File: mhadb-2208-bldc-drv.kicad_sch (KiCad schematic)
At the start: 0 parts

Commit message: schem: import STM32F103C8Tx from line sensor
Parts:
- added C10, C11, C5, C8, C9: 0u1, Capacitor_SMD:C_0402_1005Metric, symbol Device:C
- added C12, C13: 1u, Capacitor_SMD:C_0402_1005Metric, symbol Device:C
- added C14: 10n, Capacitor_SMD:C_0402_1005Metric, symbol Device:C
- added C4: 10u, Capacitor_SMD:C_0805_2012Metric, symbol Device:C
- added C6, C7: 20p, Capacitor_SMD:C_0603_1608Metric, symbol Device:C
- added D11: YELLOW, LED_SMD:LED_0805_2012Metric, symbol Device:LED
- added FB1: 600Ω@100M, Inductor_SMD:L_0805_2012Metric, symbol Device:FerriteBead
- added J2, J4: Conn_01x04_Pin, Connector_PinHeader_2.54mm:PinHeader_1x04_P2.54mm_Vertical, symbol Connector:Conn_01x04_Pin
- added R4: 10k, Resistor_SMD:R_0402_1005Metric, symbol Device:R
- added R5: 560, Resistor_SMD:R_0603_1608Metric, symbol Device:R_Small
- added R6: 5k1, Resistor_SMD:R_0402_1005Metric, symbol Device:R
- added TP4, TP5, TP6, TP7: TestPoint, TestPoint:TestPoint_Pad_D2.0mm, symbol Connector:TestPoint
- added U3: STM32F103C8Tx, Package_QFP:LQFP-48_7x7mm_P0.5mm, symbol MCU_ST_STM32F1:STM32F103C8Tx
- added Y1: 8M, Crystal:Crystal_SMD_5032-2Pin_5.0x3.2mm, symbol Device:Crystal
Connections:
- new net: R6.1, U3.38 (PA15)
- new net: D11.2 (A), R6.2
- new net: J2.3 (Pin_3), U3.21 (PB10)
- new net: J2.4 (Pin_4), U3.22 (PB11)
- new net: J2.1 (Pin_1), U3.45 (PB8)
- new net: J2.2 (Pin_2), U3.46 (PB9)
- new net: C13.1, C14.1, FB1.1, TP6.1, U3.9 (VDDA)
- new net +3V3: C10.1, C11.1, C12.1, C4.1, C8.1, C9.1, FB1.2, J4.1 (Pin_1), U3.1 (VBAT), U3.24 (VDD), U3.36 (VDD), U3.48 (VDD)
- new net BOOT: R4.2, U3.44 (BOOT0)
- new net BTN1: U3.43 (PB7)
- new net BTN2: U3.42 (PB6)
- new net CAN_RX: U3.32 (PA11)
- new net CAN_TX: U3.33 (PA12)
- new net GND: C10.2, C11.2, C12.2, C13.2, C14.2, C4.2, C5.2, C6.2, C7.2, C8.2, C9.2, D11.1 (K), J4.3 (Pin_3), R4.1, U3.23 (VSS), U3.35 (VSS), U3.47 (VSS), U3.8 (VSSA)
- new net LS1: TP7.1, U3.10 (PA0)
- new net LS10: TP4.1, U3.19 (PB1)
- new net LS2: U3.11 (PA1)
- new net LS3: U3.12 (PA2)
- new net LS4: U3.13 (PA3)
- new net LS5: U3.14 (PA4)
- new net LS6: U3.15 (PA5)
- new net LS7: U3.16 (PA6)
- new net LS8: U3.17 (PA7)
- new net LS9: U3.18 (PB0)
- new net NRST: C5.1, TP5.1, U3.7 (NRST)
- new net RGB1: U3.25 (PB12)
- new net RGB2: U3.26 (PB13)
- new net SWCLK: U3.37 (PA14)
- new net SWDIO: U3.34 (PA13)
- new net SWO: U3.39 (PB3)
- new net U0RXD: J4.2 (Pin_2), U3.31 (PA10)
- new net U0TXD: J4.4 (Pin_4), U3.30 (PA9)
- new net XTAL_I: C6.1, U3.5 (PD0), Y1.2
- new net XTAL_O: R5.2, U3.6 (PD1)
- new net XTAL_RO: C7.1, R5.1, Y1.1
- no-connect marks 0 -> 9
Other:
- note added: "CAN Alive"
- note added: "HSE"
- note added: "UART"

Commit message: schem: add buttons
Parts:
- removed TP4, TP7: TestPoint, TestPoint:TestPoint_Pad_D2.0mm, symbol Connector:TestPoint
- added SW1, SW4: SW_Push, Button_Switch_SMD:SW_SPST_TS-1088-xR020, symbol Switch:SW_Push
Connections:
- net +3V3: now also SW1.1
- net BOOT: now also SW1.2
- net GND: now also SW4.1
- net NRST: now also SW4.2
- net BTN1: no longer names the net of U3.43 (PB7)
- net BTN2: no longer names the net of U3.42 (PB6)
- net LS1: no longer names the net of U3.10 (PA0)
- net LS10: no longer names the net of U3.19 (PB1)
- net LS2: no longer names the net of U3.11 (PA1)
- net LS3: no longer names the net of U3.12 (PA2)
- net LS4: no longer names the net of U3.13 (PA3)
- net LS5: no longer names the net of U3.14 (PA4)
- net LS6: no longer names the net of U3.15 (PA5)
- net LS7: no longer names the net of U3.16 (PA6)
- net LS8: no longer names the net of U3.17 (PA7)
- net LS9: no longer names the net of U3.18 (PB0)
- net RGB2: no longer names the net of U3.26 (PB13)
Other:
- note added: "Buttons"

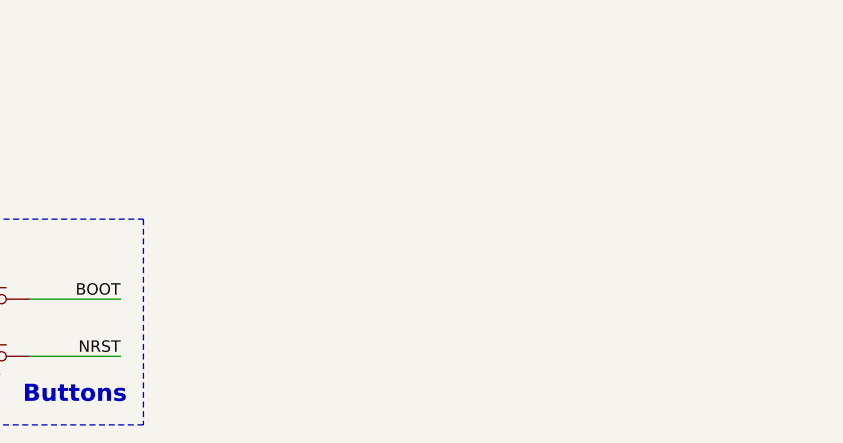
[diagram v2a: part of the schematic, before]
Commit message: schem: add CAN/Power connector
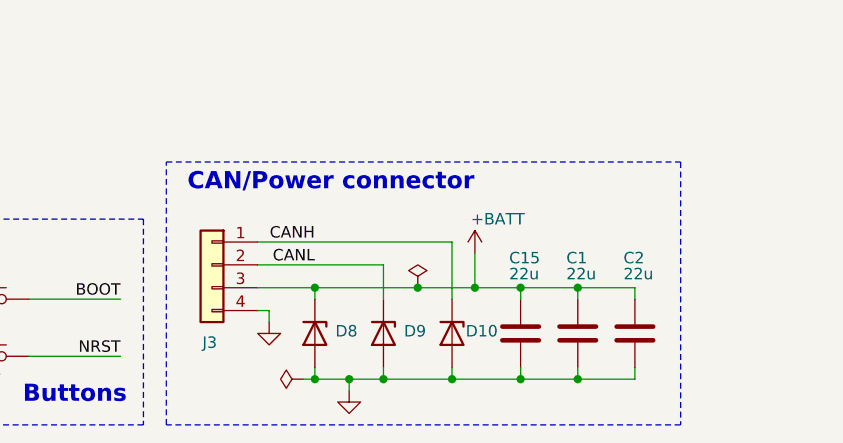
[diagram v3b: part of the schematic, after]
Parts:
- added C1, C15, C2: 22u, Capacitor_SMD:C_1206_3216Metric, symbol Device:C
- added D10, D8, D9: H5VU10U, GLCS:Diode_DFN1006, symbol GLCS:H5VU10U
- added J3: Conn_01x04, Connector_JST:JST_PH_S4B-PH-K_1x04_P2.00mm_Horizontal, symbol Connector_Generic:Conn_01x04
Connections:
- net GND: now also C1.2, C15.2, C2.2, D10.2 (A), D8.2 (A), D9.2 (A), J3.4 (Pin_4)
- new net +BATT: C1.1, C15.1, C2.1, D8.1 (K), J3.3 (Pin_3)
- new net CANH: D10.1 (K), J3.1 (Pin_1)
- new net CANL: D9.1 (K), J3.2 (Pin_2)
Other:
- note added: "CAN/Power connector"

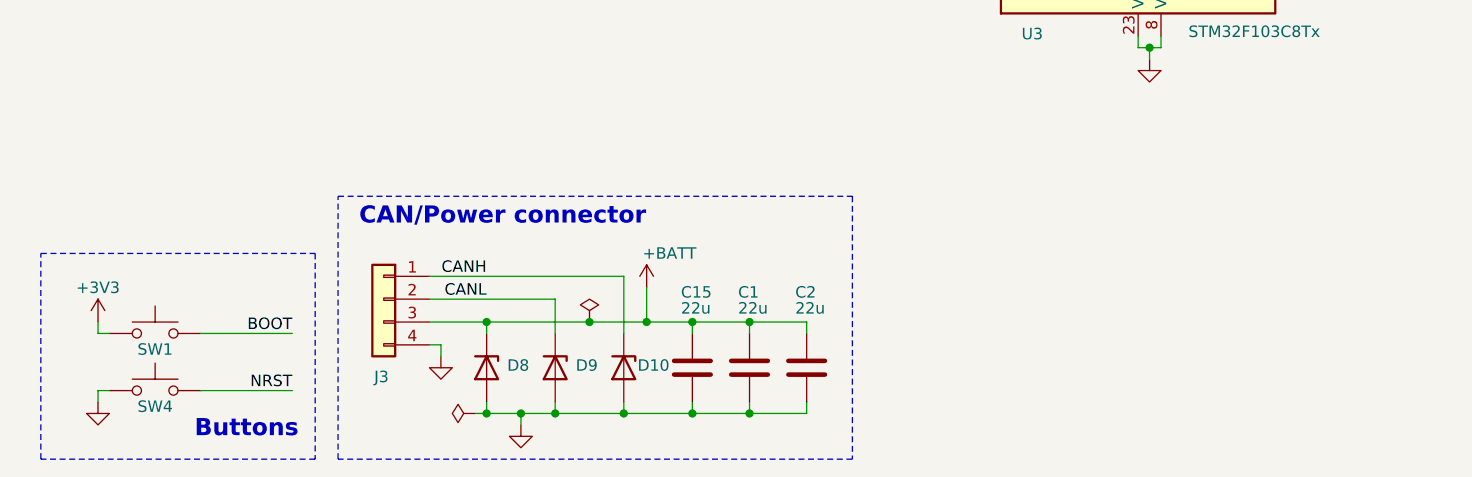
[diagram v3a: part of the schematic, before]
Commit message: schem: add CAN transceiver
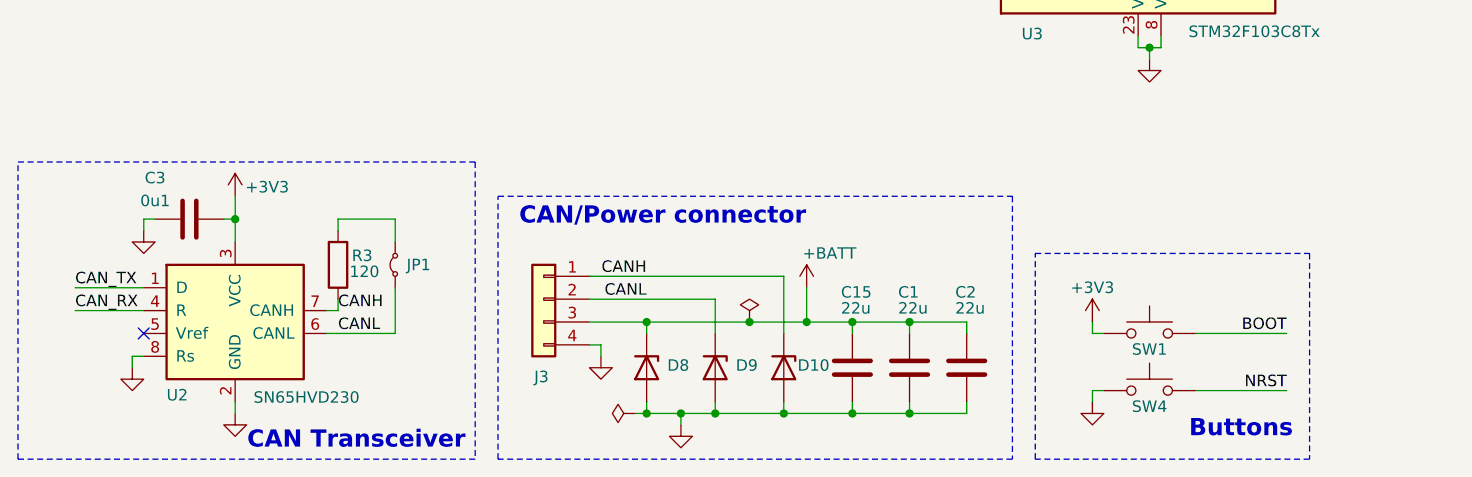
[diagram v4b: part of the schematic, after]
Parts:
- added C3: 0u1, Capacitor_SMD:C_0402_1005Metric, symbol Device:C
- added JP1: Jumper_2_Small_Bridged, Jumper:SolderJumper-2_P1.3mm_Open_RoundedPad1.0x1.5mm, symbol Jumper:Jumper_2_Small_Bridged
- added R3: 120, Resistor_SMD:R_1206_3216Metric, symbol Device:R
- added U2: SN65HVD230, Package_SO:SOIC-8_3.9x4.9mm_P1.27mm, symbol Interface_CAN_LIN:SN65HVD230
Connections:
- net +3V3: now also C3.1, U2.3 (VCC)
- net CANH: now also R3.1, U2.7 (CANH)
- net CANL: now also JP1.1 (A), U2.6 (CANL)
- net CAN_RX: now also U2.4 (R)
- net CAN_TX: now also U2.1 (D)
- net GND: now also C3.2, U2.2 (GND), U2.8 (Rs)
- new net: JP1.2 (B), R3.2
- no-connect marks 9 -> 10
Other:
- note added: "CAN Transceiver"
- moved on the sheet: C1, C15, C2, D10, D8, D9, J3, SW1, SW4

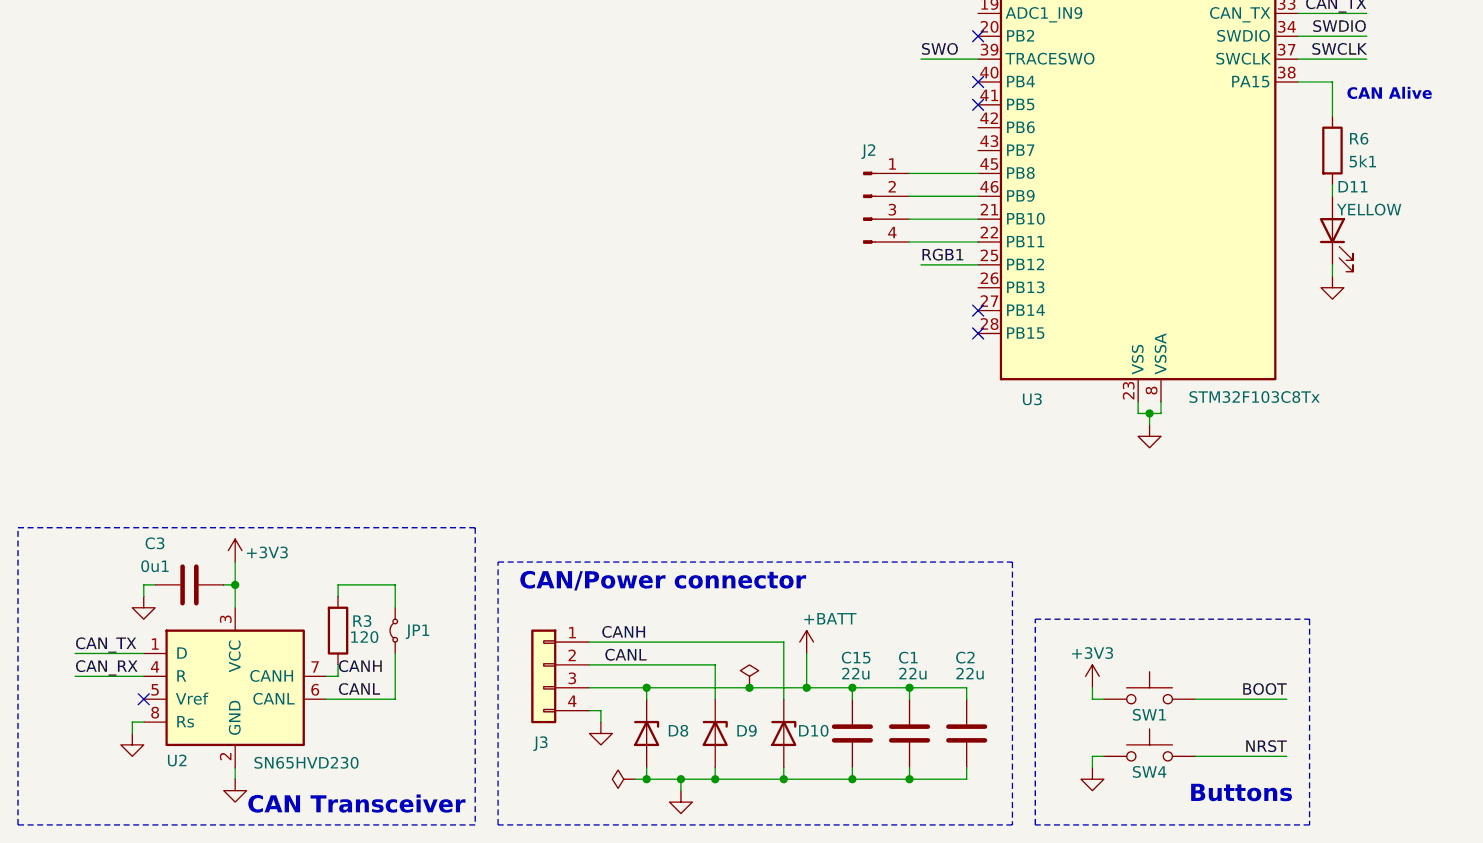
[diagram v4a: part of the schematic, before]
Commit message: schem: add SWD tag connect
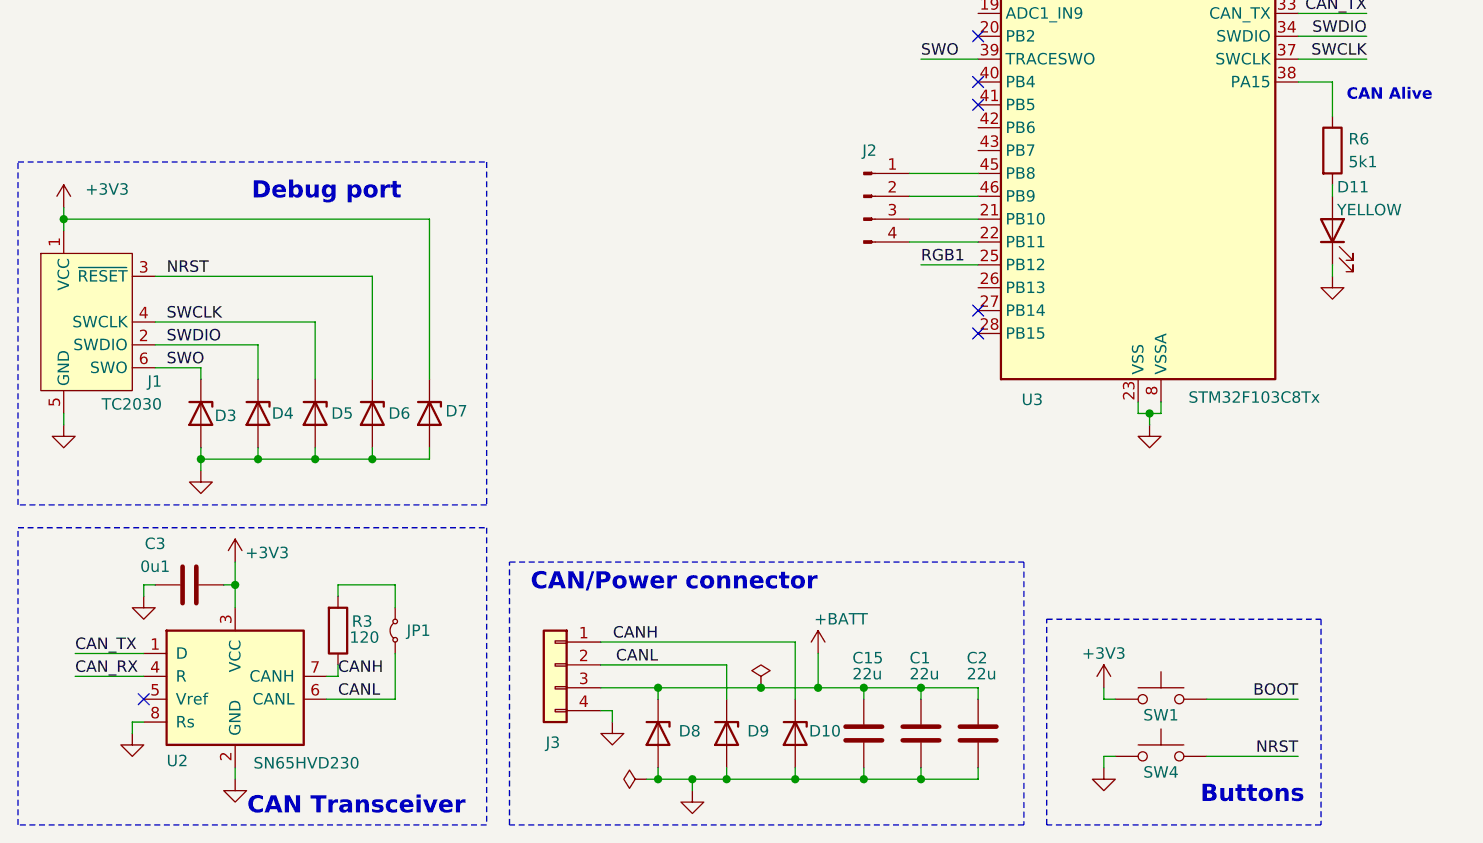
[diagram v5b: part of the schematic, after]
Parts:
- added D3, D4, D5, D6, D7: H5VU10U, GLCS:Diode_DFN1006, symbol GLCS:H5VU10U
- added J1: TC2030, Connector:Tag-Connect_TC2030-IDC-NL_2x03_P1.27mm_Vertical, symbol Connector:Conn_ARM_SWD_TagConnect_TC2030-NL
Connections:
- net +3V3: now also D7.1 (K), J1.1 (VCC)
- net GND: now also D3.2 (A), D4.2 (A), D5.2 (A), D6.2 (A), D7.2 (A), J1.5 (GND)
- net NRST: now also D6.1 (K), J1.3 (~{RESET})
- net SWCLK: now also D5.1 (K), J1.4 (SWCLK)
- net SWDIO: now also D4.1 (K), J1.2 (SWDIO)
- net SWO: now also D3.1 (K), J1.6 (SWO)
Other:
- note added: "Debug port"
- moved on the sheet: C1, C15, C2, D10, D8, D9, J3, SW1, SW4

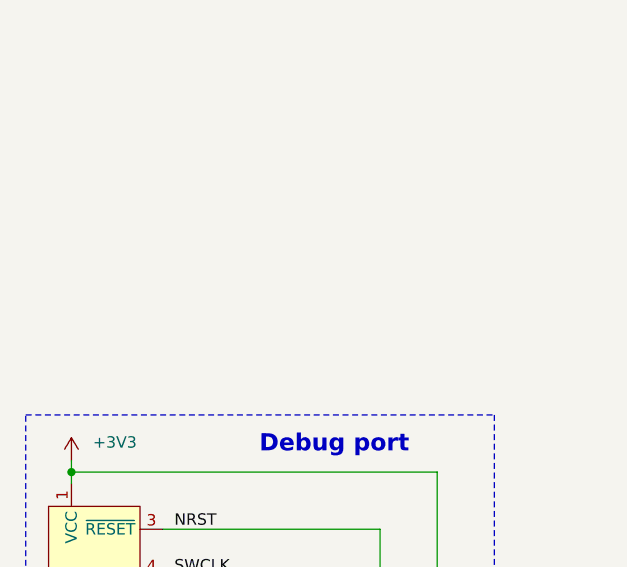
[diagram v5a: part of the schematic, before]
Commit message: schem: add HT753-1 3V3 LDO
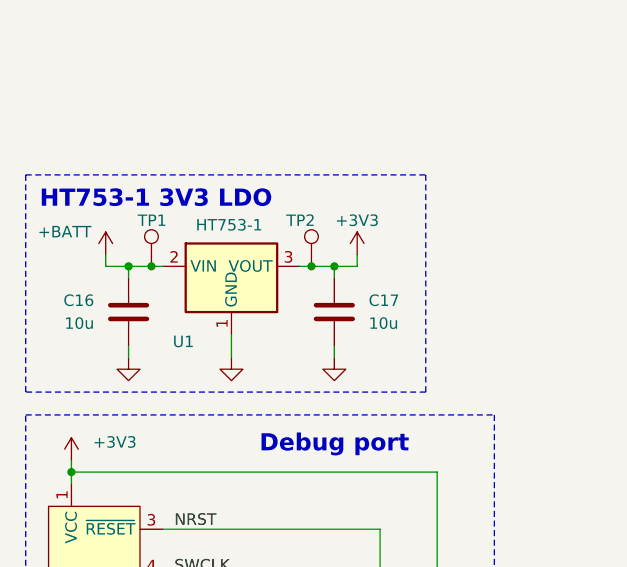
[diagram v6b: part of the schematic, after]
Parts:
- added C16, C17: 10u, Capacitor_SMD:C_0805_2012Metric, symbol Device:C
- added TP1, TP2: TestPoint, TestPoint:TestPoint_Pad_D2.0mm, symbol Connector:TestPoint
- added U1: HT753-1, Package_TO_SOT_SMD:SOT-89-3, symbol Regulator_Linear:HT75xx-1-SOT89
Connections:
- net +3V3: now also C17.1, TP2.1, U1.3 (VOUT)
- net +BATT: now also C16.1, TP1.1, U1.2 (VIN)
- net GND: now also C16.2, C17.2, U1.1 (GND)
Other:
- note added: "HT753-1 3V3 LDO"
